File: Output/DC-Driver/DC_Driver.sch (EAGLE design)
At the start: 6 parts, among them IC3 BD6231F

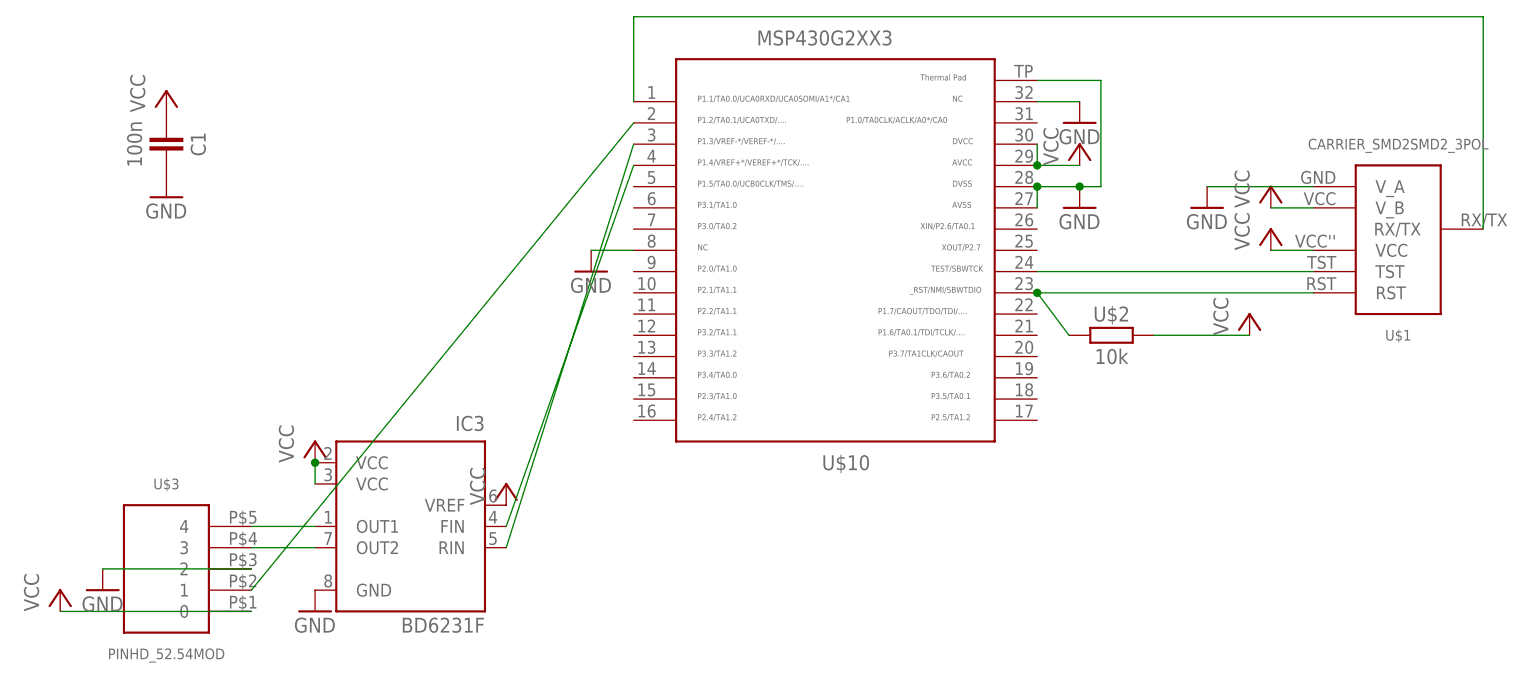
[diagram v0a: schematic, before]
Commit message: Update Pinheader
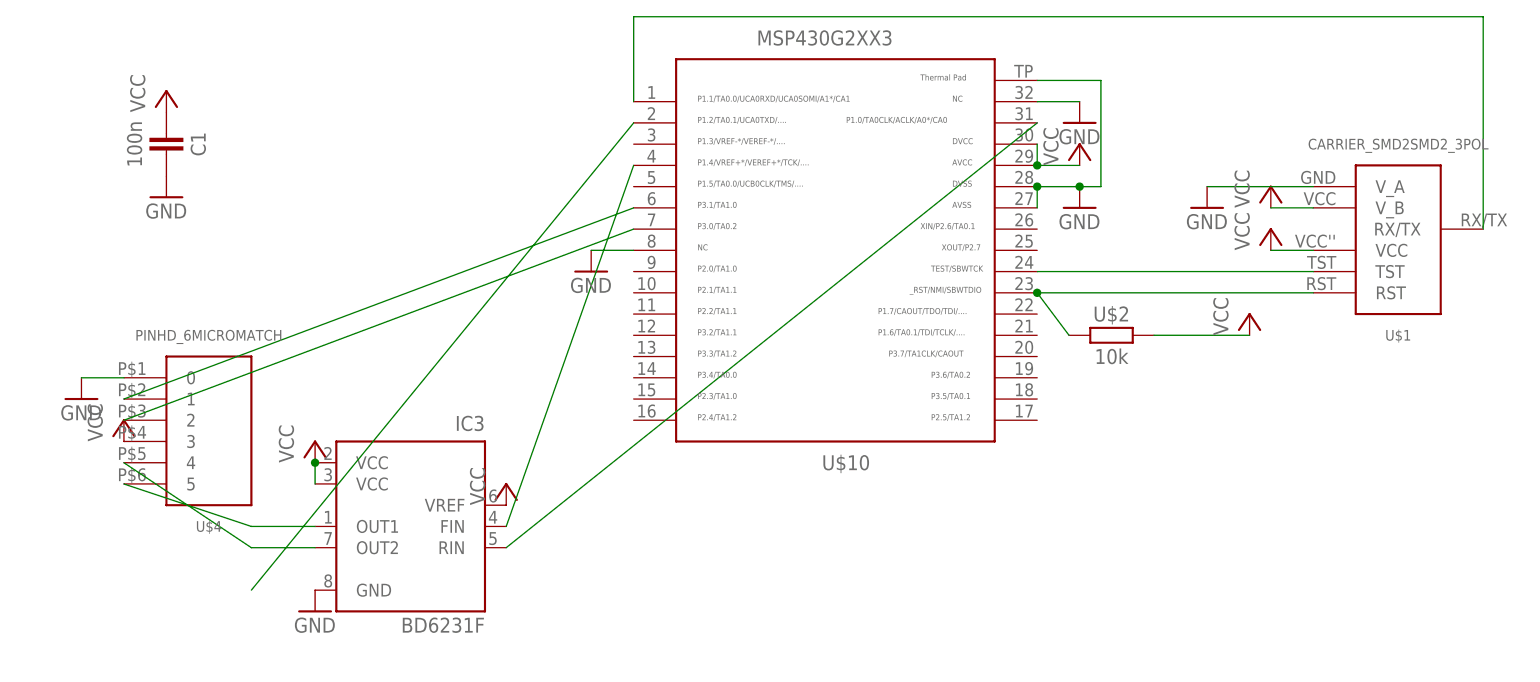
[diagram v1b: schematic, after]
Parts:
- removed U$3: PINHD_52.54MOD, thar:PINHD_52.54MOD
- added U$4: PINHD_6MICROMATCH, thar:PINHD_6MICROMATCH
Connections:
- new net N$13: U$10.6, U$4.1
- new net N$14: U$10.7, U$4.2
- net GND: now also U$4.0; no longer U$3.2
- net N$11: no longer U$3.1
- net N$2: now also U$4.4; no longer U$3.3
- net N$5: now also U$4.5; no longer U$3.4
- net N$7: now also U$10.31; no longer U$10.3
- net VCC: now also U$4.3; no longer U$3.0
